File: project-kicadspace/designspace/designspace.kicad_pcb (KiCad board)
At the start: 2 copper layers, 68 x 64 mm, 42 parts, among them J1 PJ-313B

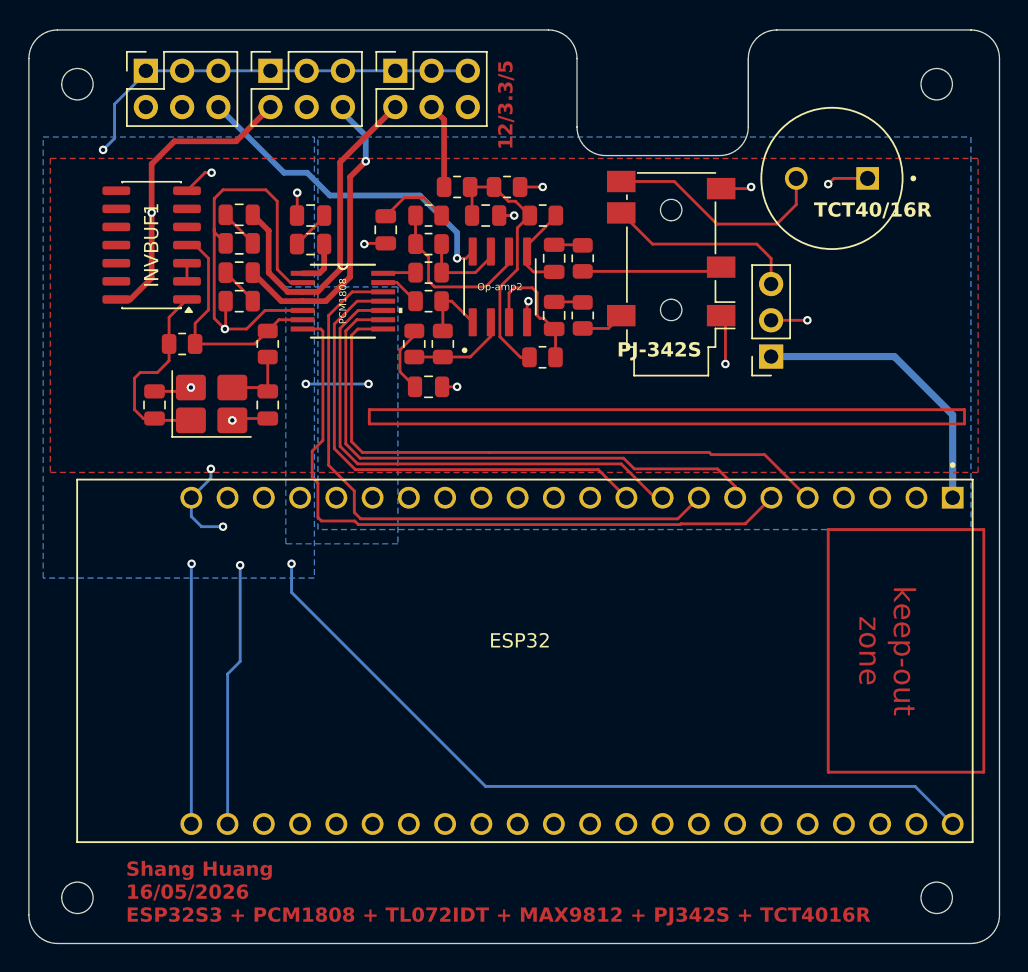
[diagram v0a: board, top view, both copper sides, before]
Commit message: feat(pcb): adjust routing for pcm1808 & update version
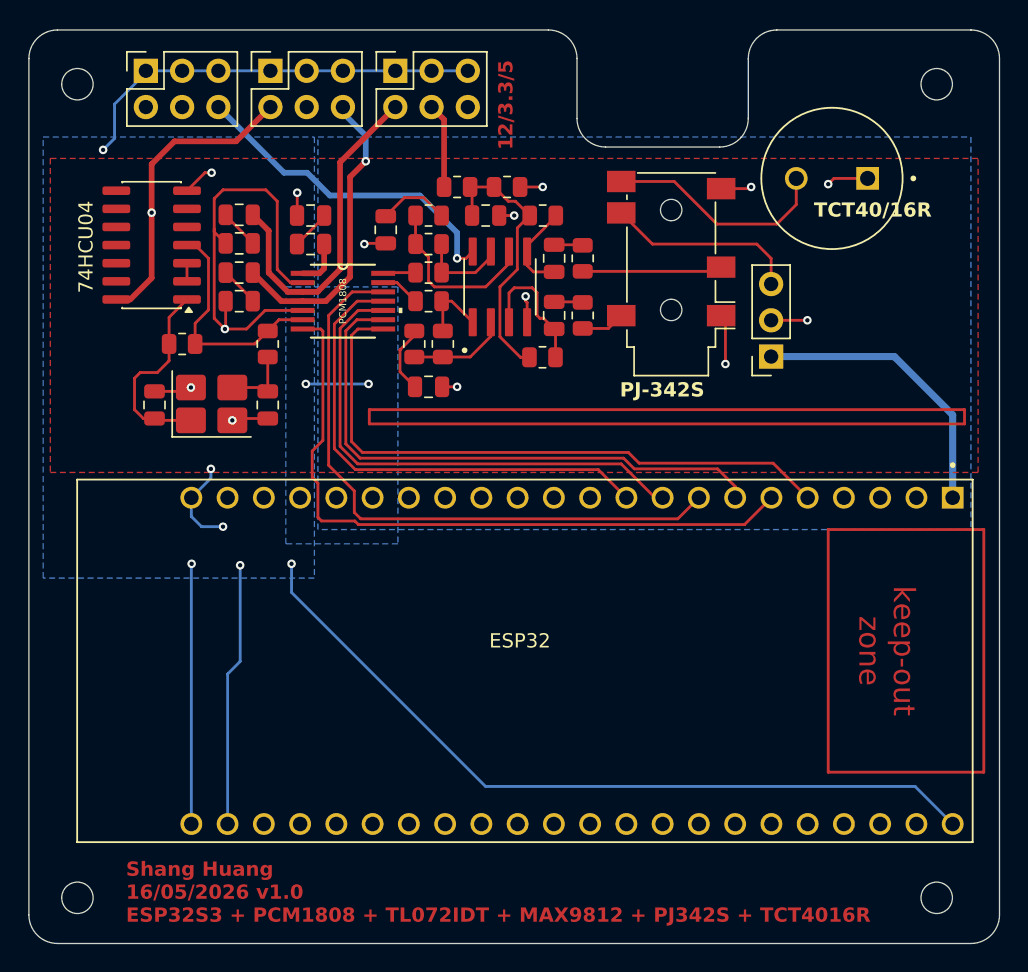
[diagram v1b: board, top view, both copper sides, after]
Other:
- outline, holes or cut-outs redrawn
- board text added: "Shang Huang 16/05/2026 v1.0 ESP32S3 + PCM1808 + TL072IDT + MAX9812 + PJ342S + TCT4016R"
- board text removed: "Shang Huang 16/05/2026 ESP32S3 + PCM1808 + TL072IDT + MAX9812 + PJ342S + TCT4016R"
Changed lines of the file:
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@@
 			(at 0 0 0)
 			(layer "F.SilkS")
+			(hide yes)
 			(effects
 				(font
@@
 			(at 0 0 0)
 			(layer "F.Fab")
-			(hide yes)
 			(effects
 				(font
@@
 		)
 		(property "Value" "74HCU04"
-			(at 0 5.28 180)
-			(layer "F.Fab")
-			(hide yes)
+			(at 4.6 -0.13 270)
+			(layer "F.SilkS")
 			(effects
 				(font
@@
 			(layer "F.Fab")
 		)
-		(fp_text user "${REFERENCE}"
-			(at 0 0 270)
-			(layer "F.SilkS")
-			(effects
-				(font
-					(size 1 1)
-					(thickness 0.15)
-				)
-			)
-		)
 		(pad "1" smd roundrect
 			(at -2.475 -3.81 180)
@@
 	)
 	(gr_line
-		(start 84.4 66.8)
-		(end 92.4 66.8)
+		(start 84.4 66.2)
+		(end 92.4 66.2)
 		(stroke
 			(width 0.05)
@@
 	(gr_line
 		(start 94.4 60)
-		(end 94.4 64.8)
+		(end 94.4 64.2)
 		(stroke
 			(width 0.05)
@@
 	)
 	(gr_arc
-		(start 84.4 66.8)
-		(mid 82.985786 66.214214)
-		(end 82.4 64.8)
+		(start 84.4 66.2)
+		(mid 82.985786 65.614214)
+		(end 82.4 64.2)
 		(stroke
 			(width 0.05)
@@
 	)
 	(gr_arc
-		(start 94.4 64.8)
-		(mid 93.814214 66.214214)
-		(end 92.4 66.8)
+		(start 94.4 64.2)
+		(mid 93.814214 65.614214)
+		(end 92.4 66.2)
 		(stroke
 			(width 0.05)
@@
 	(gr_line
 		(start 82.4 60)
-		(end 82.4 64.8)
+		(end 82.4 64.2)
 		(stroke
 			(width 0.05)
@@
 		(layer "Edge.Cuts")
 	)
-	(gr_text "Shang Huang\n16/05/2026\nESP32S3 + PCM1808 + TL072IDT + MAX9812 + PJ342S + TCT4016R"
+	(gr_text "Shang Huang\n16/05/2026 v1.0\nESP32S3 + PCM1808 + TL072IDT + MAX9812 + PJ342S + TCT4016R"
 		(at 50.8 120.6 0)
 		(layer "F.Cu")
@@
 	)
 	(gr_text "PJ-342S"
-		(at 85.2 81 0)
+		(at 85.4 83.8 0)
 		(layer "F.SilkS")
 		(effects
@@
 	)
 	(segment
+		(start 78.8 76.6625)
+		(end 78.8 76.99)
+		(width 0.2)
+		(layer "F.Cu")
+		(net 2)
+	)
+	(segment
 		(start 56.983401 71.95)
 		(end 56.983401 69.816599)
@@
 	)
 	(segment
-		(start 78.905 77.095)
-		(end 79 77)
+		(start 76.95 71)
+		(end 78 71)
 		(width 0.2)
 		(layer "F.Cu")
@@
 	)
 	(segment
-		(start 76.95 71)
-		(end 78 71)
+		(start 56.983401 69.816599)
+		(end 57.6 69.2)
 		(width 0.2)
 		(layer "F.Cu")
@@
 	)
 	(segment
-		(start 56.983401 69.816599)
-		(end 57.6 69.2)
+		(start 78.8 76.99)
+		(end 78.905 77.095)
 		(width 0.2)
 		(layer "F.Cu")
@@
 	)
 	(segment
+		(start 78.905 77.095)
+		(end 78.905 78.475)
+		(width 0.2)
+		(layer "F.Cu")
+		(net 2)
+	)
+	(segment
 		(start 56.335 68)
 		(end 56.8 68)
@@
 	)
 	(segment
-		(start 78.905 78.475)
-		(end 78.905 77.095)
-		(width 0.2)
-		(layer "F.Cu")
-		(net 2)
-	)
-	(segment
 		(start 61.4 74.7788)
 		(end 62.3212 75.7)
@@
 	)
 	(via
-		(at 79 77)
+		(at 78.8 76.6625)
 		(size 0.6)
 		(drill 0.3)
@@
 	)
 	(segment
-		(start 76.25 87.599)
-		(end 91.6661 87.599)
+		(start 67.049999 78.950001)
+		(end 66.604 79.396)
 		(width 0.2)
 		(layer "F.Cu")
@@
 	)
 	(segment
-		(start 67.3674 87.599)
-		(end 76.25 87.599)
+		(start 66.604 79.396)
+		(end 66.604 86.8356)
 		(width 0.2)
 		(layer "F.Cu")
@@
 	)
 	(segment
-		(start 95.54 87.75)
-		(end 98.56 90.77)
+		(start 67.3674 87.599)
+		(end 85.999 87.599)
 		(width 0.2)
 		(layer "F.Cu")
@@
 	)
 	(segment
-		(start 91.8171 87.75)
-		(end 95.54 87.75)
-		(width 0.2)
-		(layer "F.Cu")
-		(net 38)
-	)
-	(segment
-		(start 66.604 79.396)
-		(end 66.604 86.8356)
+		(start 96.139 88.349)
+		(end 98.56 90.77)
 		(width 0.2)
 		(layer "F.Cu")
@@
 	)
 	(segment
-		(start 91.6661 87.599)
-		(end 91.8171 87.75)
+		(start 85.999 87.599)
+		(end 86.749 88.349)
 		(width 0.2)
 		(layer "F.Cu")
@@
 	)
 	(segment
-		(start 67.049999 78.950001)
-		(end 66.604 79.396)
+		(start 86.749 88.349)
+		(end 96.139 88.349)
 		(width 0.2)
 		(layer "F.Cu")
@@
 	)
 	(segment
-		(start 66.8329 92.4)
-		(end 64.499 92.4)
+		(start 94.139 92.651)
+		(end 96.02 90.77)
 		(width 0.2)
 		(layer "F.Cu")
@@
 	)
 	(segment
-		(start 67.0839 92.651)
-		(end 66.8329 92.4)
+		(start 66.8329 92.4)
+		(end 67.0839 92.651)
 		(width 0.2)
 		(layer "F.Cu")
@@
 	)
 	(segment
-		(start 64.25 92.151)
-		(end 64.25 89.75)
+		(start 63.1806 78.949999)
+		(end 64.449999 78.949999)
 		(width 0.2)
 		(layer "F.Cu")
@@
 	)
 	(segment
-		(start 64.449999 78.949999)
-		(end 63.1806 78.949999)
+		(start 64.25 89.75)
+		(end 64.25 92.151)
 		(width 0.2)
 		(layer "F.Cu")
@@
 	)
 	(segment
-		(start 64.599 79.099)
-		(end 64.449999 78.949999)
+		(start 64.599 86.75)
+		(end 63.849 87.5)
 		(width 0.2)
 		(layer "F.Cu")
@@
 	(segment
 		(start 63.849 87.5)
-		(end 64.599 86.75)
-		(width 0.2)
-		(layer "F.Cu")
-		(net 61)
-	)
-	(segment
-		(start 64.25 89.75)
 		(end 63.849 89.349)
 		(width 0.2)
@@
 	)
 	(segment
-		(start 64.599 86.75)
-		(end 64.599 79.099)
-		(width 0.2)
-		(layer "F.Cu")
-		(net 61)
-	)
-	(segment
-		(start 89.6771 92.6)
-		(end 89.6261 92.651)
+		(start 64.599 79.099)
+		(end 64.599 86.75)
 		(width 0.2)
 		(layer "F.Cu")
@@
 	)
 	(segment
-		(start 63.849 89.349)
-		(end 63.849 87.5)
+		(start 64.499 92.4)
+		(end 66.8329 92.4)
 		(width 0.2)
 		(layer "F.Cu")
@@
 	)
 	(segment
-		(start 94.19 92.6)
-		(end 89.6771 92.6)
+		(start 64.449999 78.949999)
+		(end 64.599 79.099)
 		(width 0.2)
 		(layer "F.Cu")
@@
 	)
 	(segment
-		(start 89.6261 92.651)
-		(end 67.0839 92.651)
+		(start 64.25 92.151)
+		(end 64.499 92.4)
 		(width 0.2)
 		(layer "F.Cu")
@@
 	)
 	(segment
-		(start 64.499 92.4)
-		(end 64.25 92.151)
+		(start 63.849 89.349)
+		(end 64.25 89.75)
 		(width 0.2)
 		(layer "F.Cu")
@@
 	)
 	(segment
-		(start 96.02 90.77)
-		(end 94.19 92.6)
+		(start 67.0839 92.651)
+		(end 94.139 92.651)
 		(width 0.2)
 		(layer "F.Cu")
